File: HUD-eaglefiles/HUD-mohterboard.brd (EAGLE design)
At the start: 97.8 x 69.8 mm, 26 parts, among them IC1 7805TV, U2 ATMEGA328P_TQFP, Y1 4MHz

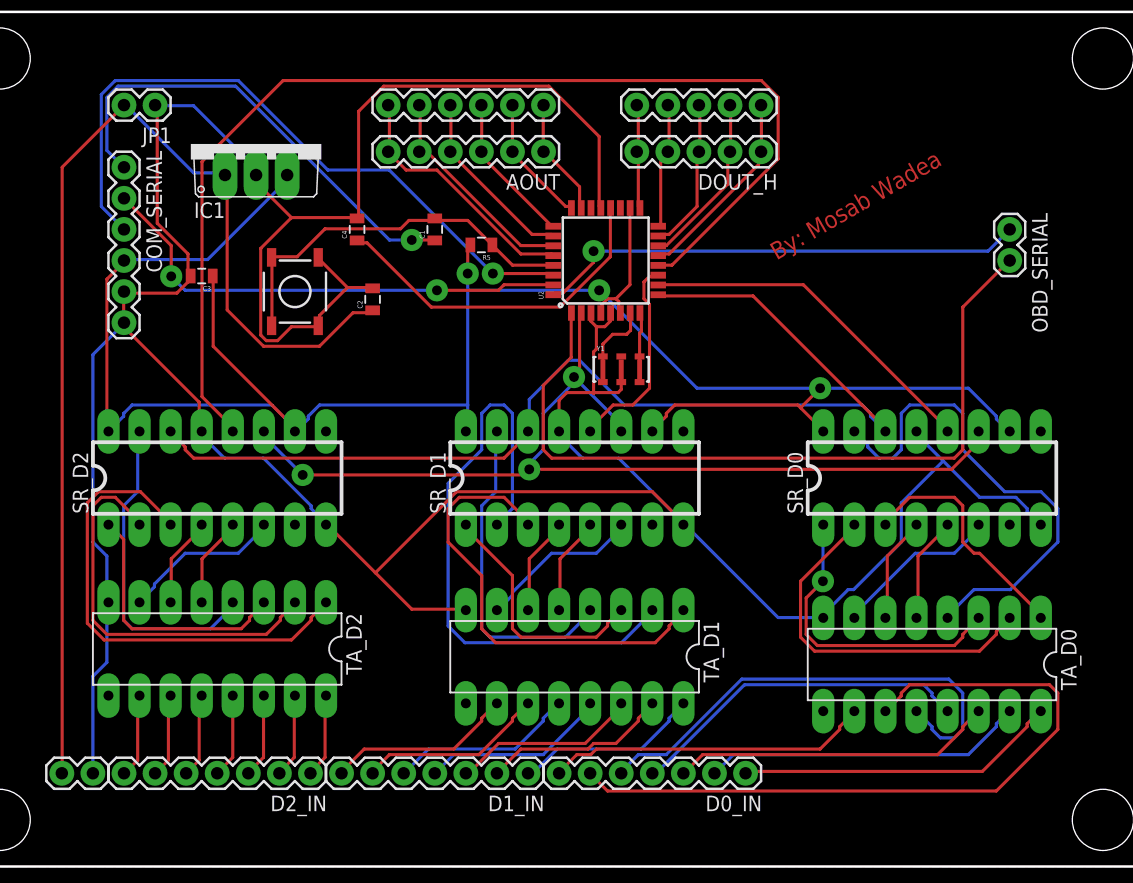
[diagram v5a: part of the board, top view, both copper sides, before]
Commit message: removed vias from under the mcu
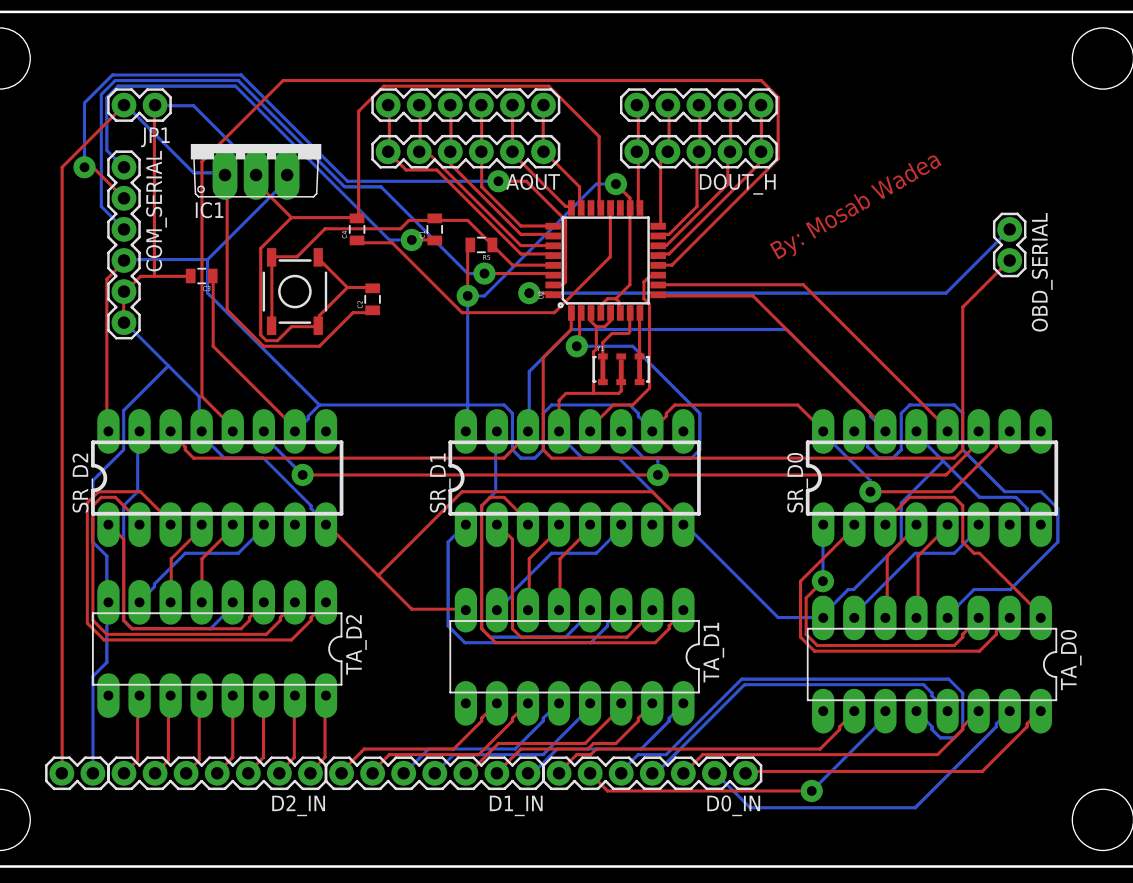
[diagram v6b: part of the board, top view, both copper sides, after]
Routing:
- net N$7: track 59.3 -> 27.7 mm, vias 0 -> 1
- net B1: track 49.6 -> 21.8 mm
- net TX: track 39.9 -> 60.9 mm
- net VCC: track 174.5 -> 182.1 mm
- net SR_CLK: track 82.6 -> 89.7 mm
- net C1: track 20.3 -> 24.8 mm
- net A1: track 37.3 -> 33.5 mm
- net GND: track 293.5 -> 289.9 mm
- net SR_SDATA: track 90.5 -> 93.9 mm
- net OBD_RX: track 40.1 -> 43.4 mm
- net N$3: track 26.3 -> 28.7 mm
- net ADC2: track 12.6 -> 13.9 mm
- net ADC3: track 15.1 -> 15.7 mm
